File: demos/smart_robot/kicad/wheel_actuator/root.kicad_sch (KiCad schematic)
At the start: 13 parts, among them M1 WHEEL_MOTOR_DESIGN_ENVELOPE, U1 AT32M416, U2 DRV8323, U3 TCAN3413DR

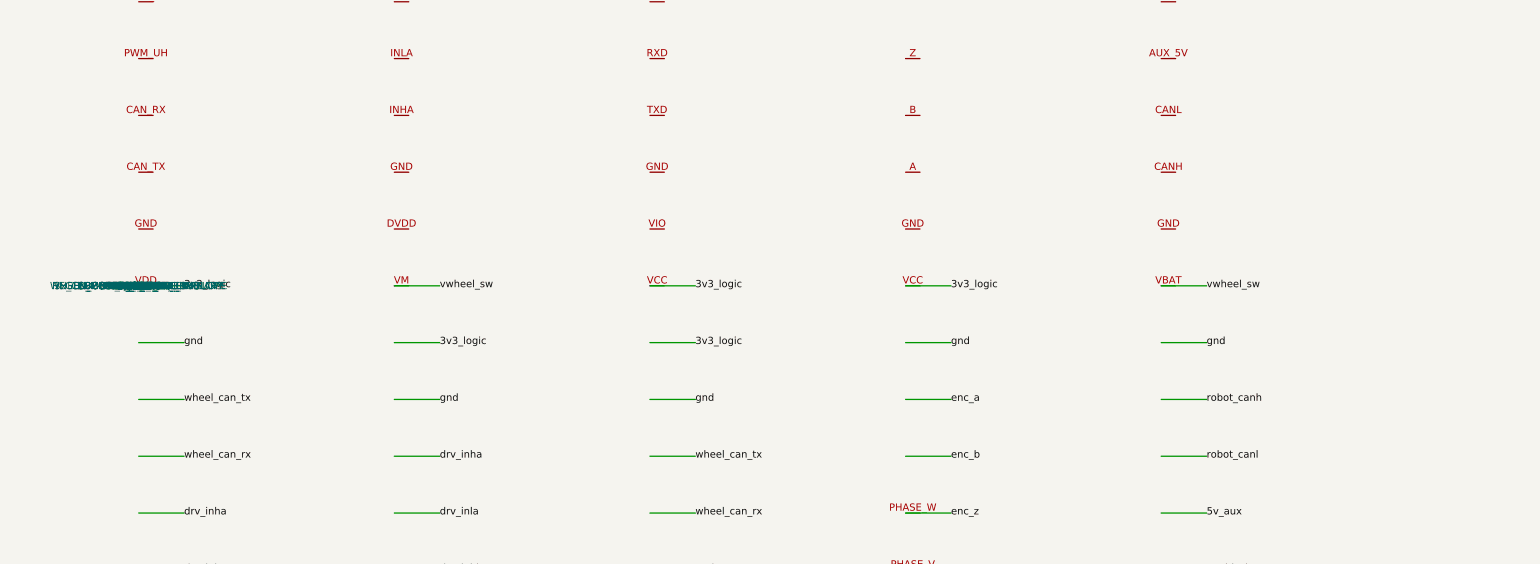
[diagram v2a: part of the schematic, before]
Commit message: Select smart robot actuator harness evidence
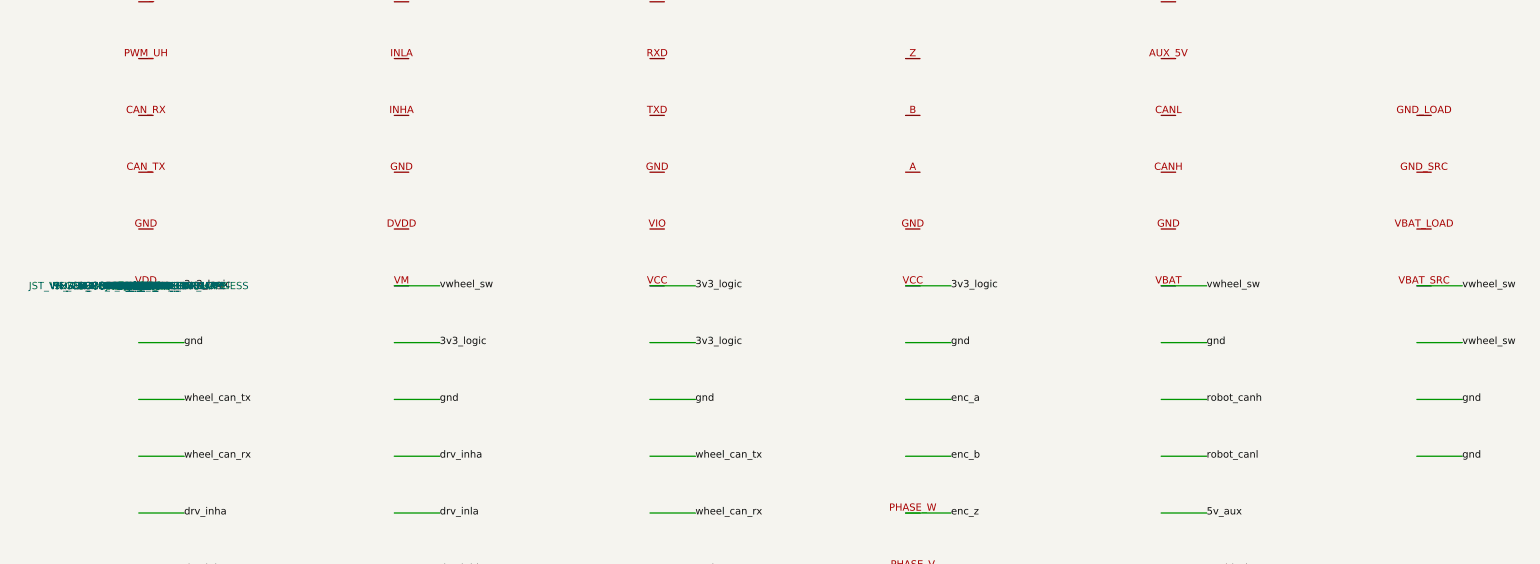
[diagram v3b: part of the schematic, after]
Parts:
- added JACT1_CABLE: JST_VH_AWG16_0P5M_ACTUATOR_HARNESS, symbol CircuitCI:Actuator_Bus_Cable
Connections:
- net vwheel_sw: now also JACT1_CABLE.VBAT_SRC
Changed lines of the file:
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@@
     (pin "VBAT") (pin "GND") (pin "CANH") (pin "CANL") (pin "AUX_5V")
     (pin "ENABLE") (pin "FAULT") (pin "SYNC"))
+  (symbol (lib_id "CircuitCI:Actuator_Bus_Cable") (at 225 0 0)
+    (property "Reference" "JACT1_CABLE")
+    (property "Value" "JST_VH_AWG16_0P5M_ACTUATOR_HARNESS")
+    (pin "VBAT_SRC") (pin "VBAT_LOAD") (pin "GND_SRC") (pin "GND_LOAD"))
+  (wire (pts (xy 225 0) (xy 233 0))) (label "vwheel_sw" (at 233 0 0))
+  (wire (pts (xy 225 10) (xy 233 10))) (label "vwheel_sw" (at 233 10 0))
+  (wire (pts (xy 225 20) (xy 233 20))) (label "gnd" (at 233 20 0))
+  (wire (pts (xy 225 30) (xy 233 30))) (label "gnd" (at 233 30 0))
   (wire (pts (xy 0 0) (xy 8 0))) (label "3v3_logic" (at 8 0 0))
   (wire (pts (xy 0 10) (xy 8 10))) (label "gnd" (at 8 10 0))

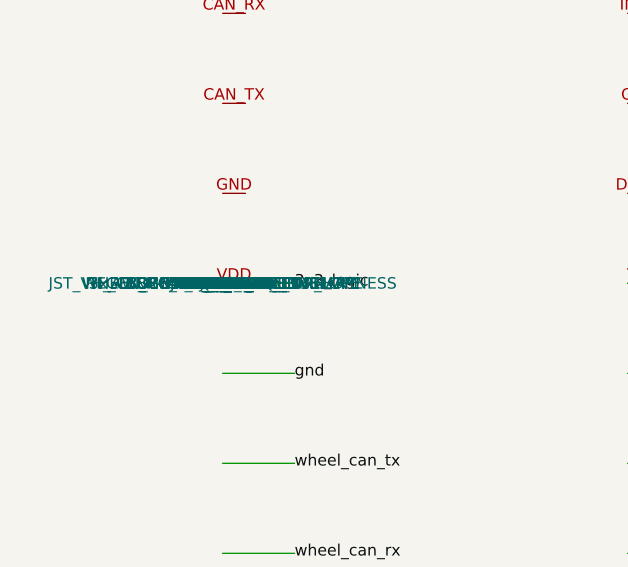
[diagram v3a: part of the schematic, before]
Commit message: Select smart robot regen absorber evidence
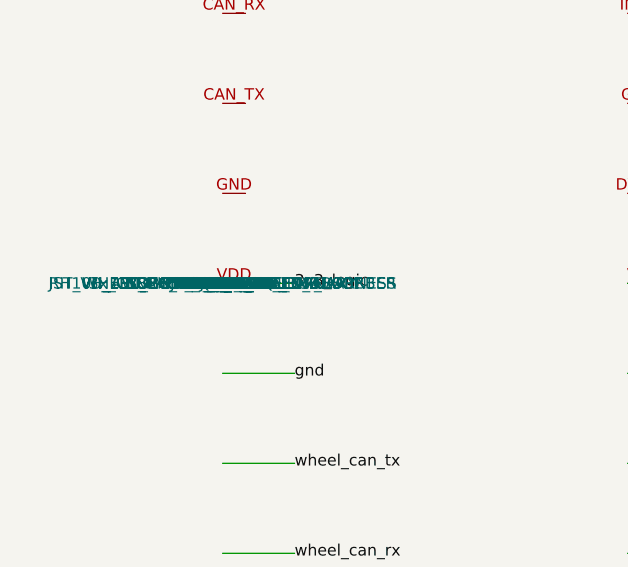
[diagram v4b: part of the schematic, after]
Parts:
- REGEN1: value REGEN_CLAMP_DESIGN_ENVELOPE -> RH100_1R0_FIRST_PASS_REGEN_ABSORBER
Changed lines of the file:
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@@
   (symbol (lib_id "CircuitCI:Regen_Clamp_Envelope") (at 180 120 0)
     (property "Reference" "REGEN1")
-    (property "Value" "REGEN_CLAMP_DESIGN_ENVELOPE")
+    (property "Value" "RH100_1R0_FIRST_PASS_REGEN_ABSORBER")
     (pin "BUS") (pin "GND"))
   (symbol (lib_id "CircuitCI:Resistor") (at 135 130 0)
